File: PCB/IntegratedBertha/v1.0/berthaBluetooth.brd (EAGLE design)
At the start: 96.7 x 71.9 mm, 55 parts, among them CON1 SPI, Q1 BSP75, Q2 BSP75, Q4 BSP75, Q7 BSP75, X3 16MHz, X4 MINI-USB

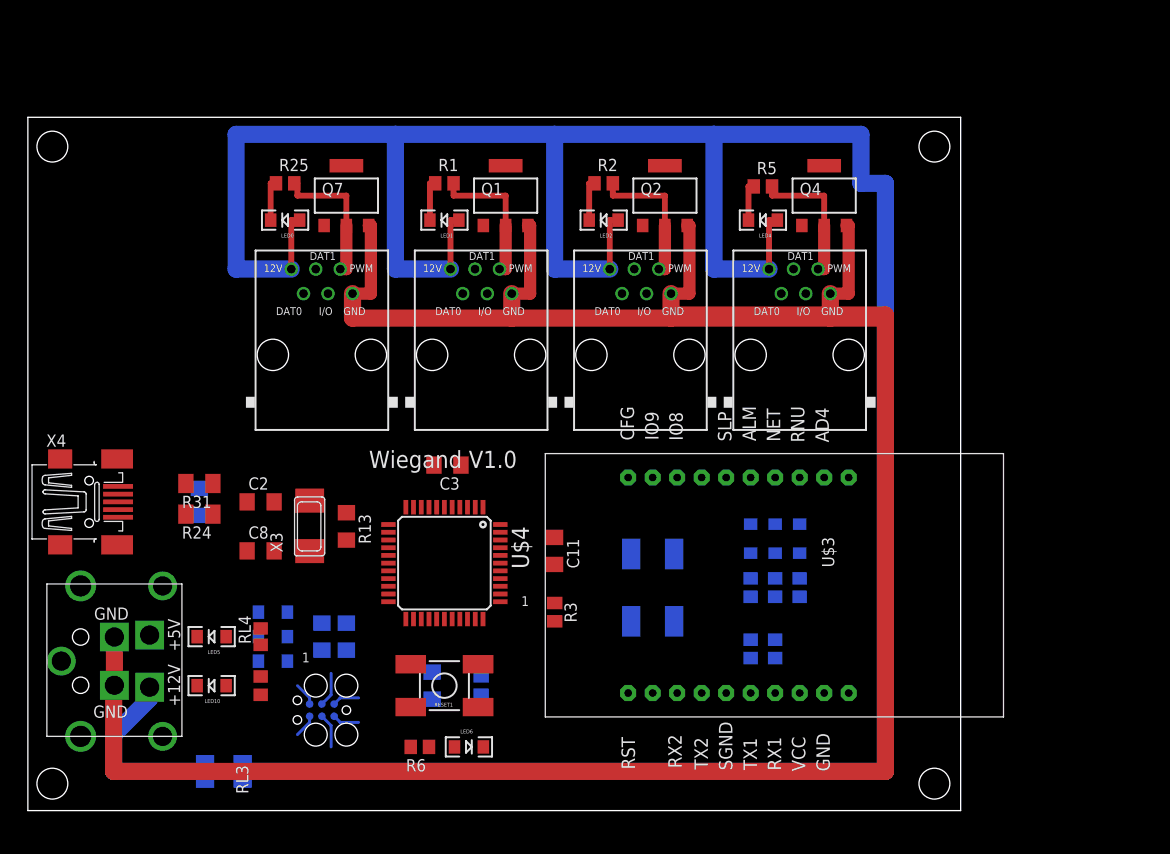
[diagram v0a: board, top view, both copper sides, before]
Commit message: Add relay card and integrated bioreactor
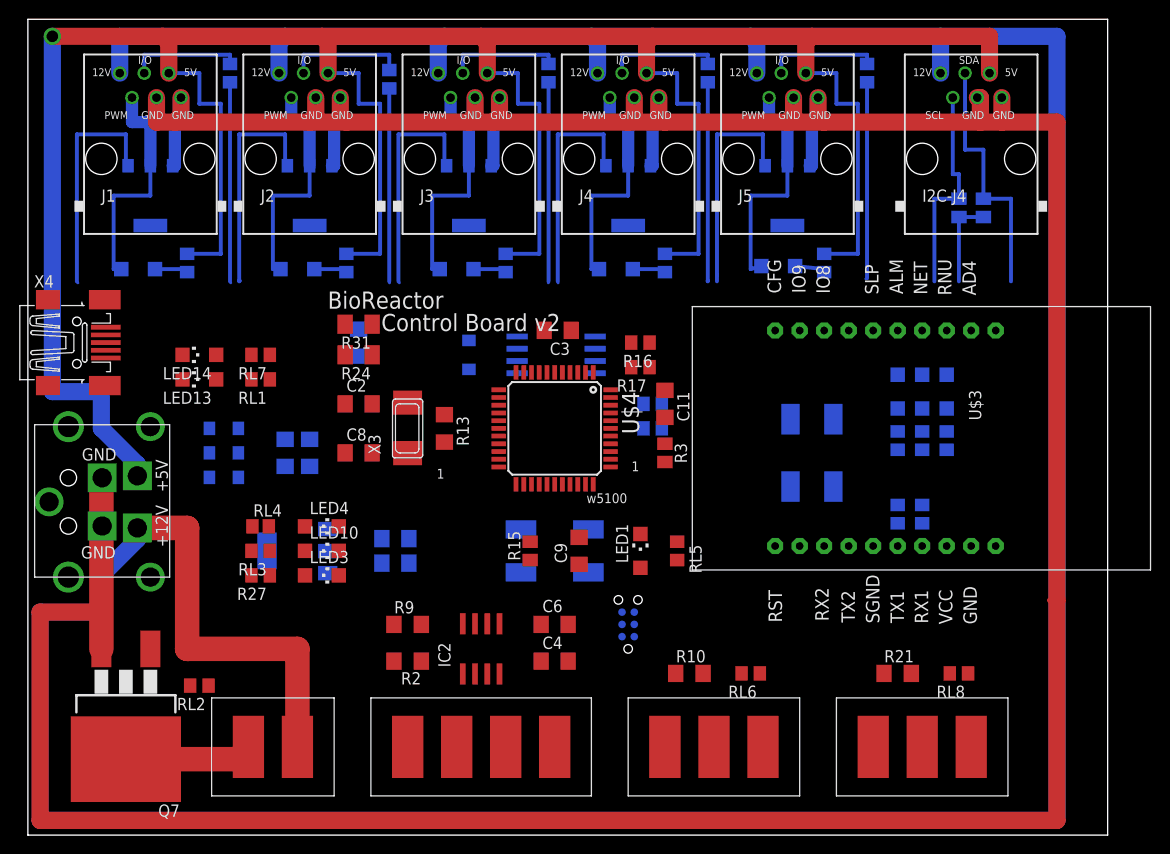
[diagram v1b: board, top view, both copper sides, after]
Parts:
- removed DOOR0, DOOR1, DOOR2, DOOR4: RJ12, lpatiny:RJ12-STRAIGHT-WIEGAND
- removed F1: 0.5A, lpatiny:C1812
- removed LED0: Blue, SparkFun:LED-1206
- added C1, C5: 10uF, rcl:C1206
- added C4: 100nF, rcl:C1206
- added C6: 330nF, rcl:C1206
- added D5: 1N581D1206, lpatiny:LED-1206
- added I2C-J4: RJ12STRAIGHT-I2C, lpatiny:RJ12-STRAIGHT-I2C
- added IC1: REG1117, burr-brown:SOT223
- added IC2: AD8223, analog-devices:SO8
- added J1, J2, J3, J4, J5: RJ12, lpatiny:RJ12-STRAIGHT
- added J7: 22--02, lpatiny:2-PIN-5.08S
- added LED13, LED3: RED, adafruit:CHIPLED_1206
- added LED14: GREEN, adafruit:CHIPLED_1206
- added LED7: BLue, adafruit:CHIPLED_1206
- added LED8: Blue, adafruit:CHIPLED_1206
- added Q5, Q6: BSP75, infineon:PG-SOT-223
- added R, R17, R32, R33, R34, R35, R4, R7: 1k, rcl:R0805
- added R10, R21: 4.7k, resistor:R1206
- added R16, R18: 10k, rcl:R0805
- added R27, RL1, RL2, RL5, RL6, RL7, RL8: 1K, rcl:R0805
- added R28, R29: 10K, resistor:M0805
- added R9: 100, resistor:R1206
- added U$1: SST25VF064C, BertaLib:SOIC_8-LEAD
- added X1: 22-23-20415.08S, lpatiny:4-PIN-5.08S
- added X2, X5: 22-23-20315.08S, lpatiny:3-PIN-5.08S
- CON1: device lpatiny:TC2030-MCP -> lpatiny:TC2030-MCP-NL
- LED1: value Blue -> GREEN; device SparkFun:LED-1206 -> adafruit:CHIPLED_1206
- LED10, LED11, LED12, LED2, LED9: device SparkFun:LED-1206 -> adafruit:CHIPLED_1206
- LED4: value Blue -> RED; device SparkFun:LED-1206 -> adafruit:CHIPLED_1206
- LED5, LED6: value RED -> Blue; device SparkFun:LED-1206 -> adafruit:CHIPLED_1206
- Q7: value BSP75 -> IRF3704S; device infineon:PG-SOT-223 -> transistor-power:D2PACK
- R2: value 10k -> 300; device rcl:R0805 -> resistor:R1206
- R25, R5: value 10k -> 1k
- R6: value 1K -> 1k
- U$4: value ATMEGA32U4 -> ATMEGA32U4-AU
- moved Q7 60.4 mm to (10.2, 7.62), turned to 180 degrees
- moved R6 56.2 mm to (66.0, 56.5), flipped to the bottom, turned to 90 degrees
- moved LED4 55.7 mm to (30.5, 29.2), turned to 270 degrees
- moved R2 53.5 mm to (39.4, 15.2), turned to 180 degrees
- moved LED6 49.5 mm to (44.5, 55.9), flipped to the bottom, turned to 270 degrees
- moved LED2 48.5 mm to (11.4, 55.9), flipped to the bottom, turned to 270 degrees
- moved LED1 39.9 mm to (63.5, 26.7), turned to 0 degrees
- moved LED5 39.1 mm to (27.9, 55.9), flipped to the bottom, turned to 270 degrees
- moved Q2 36.8 mm to (29.2, 63.5), flipped to the bottom, turned to 180 degrees
- moved Q1 36.8 mm to (12.7, 63.5), flipped to the bottom, turned to 180 degrees
- moved Q4 36.8 mm to (45.7, 63.5), flipped to the bottom, turned to 180 degrees
- moved R1 33.3 mm to (64.8, 39.4), flipped to the bottom, turned to 180 degrees
- moved CON1 29.9 mm to (62.2, 16.5), turned to 90 degrees
- moved R5 27.8 mm to (49.5, 56.5), flipped to the bottom, turned to 90 degrees
- moved R24 23.3 mm to (34.3, 47.0)
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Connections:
- removed net +5V1: R6.2
- removed net D2*: DOOR0.DAT0, U$4.19
- removed net D3*: DOOR0.DAT1, U$4.18
- removed net N$31: DOOR4.PWM, Q4.2, R5.2
- removed net N$39: F1.1, U$6.+12V
- new net 3.3V: C1.1, IC1.2, R1.2, R16.2, R27.2, U$1.RST/HOLD, U$1.VDD, U$1.WP
- new net DIFF+: IC2.3, X1.3
- new net DIFF-: IC2.2, X1.2
- new net FMOSI: D5.A, R1.1, U$1.SI
- new net N$10: R16.1, R17.1, U$1.CE
- new net N$13: IC2.1, R2.2
- new net N$14: LED14.A, RL7.2
- new net N$15: IC2.8, R2.1
- new net N$17: LED2.A, R25.1
- new net N$18: J1.I/O, R.2
- new net N$19: J5.PWM, LED8.C, Q6.2
- new net N$20: LED3.A, R27.1
- new net N$21: R10.2, RL6.2, X2.2
- new net N$22: LED6.A, R5.1
- new net N$28: J2.PWM, LED5.C, Q2.2
- new net N$29: J4.I/O, R34.2
- new net N$30: LED7.A, R6.1
- new net N$32: J5.I/O, R35.2
- new net N$33: LED8.A, R7.1
- new net N$34: J1.PWM, LED2.C, Q1.2
- new net N$36: J7.2, Q7.2
- new net N$4: LED5.A, R4.1
- new net N$40: IC2.6, R9.1
- new net N$8: LED13.A, RL1.2
- new net SCL: I2C-J4.SCL, R28.2, U$4.18
- new net SDA: I2C-J4.SDA, R29.2, U$4.19
- net +12V: now also I2C-J4.+12V, J1.+12V, J2.+12V, J3.+12V, J4.+12V, J5.+12V, J7.1, U$6.+12V; no longer DOOR0.+12V, DOOR1.+12V, DOOR2.+12V, DOOR4.+12V, F1.2, LED0.A, LED1.A, LED2.A, LED4.A
- net +5V: now also C4.1, I2C-J4.+5V, IC2.7, J1.+5V, J2.+5V, J3.+5V, J4.+5V, J5.+5V, R10.1, R21.1, R25.2, R28.1, R29.1, R4.2, R5.2, R6.2, R7.2, X1.1, X2.1, X5.1
- net +5V/1: now also C5.1, IC1.3
- net A0: now also R35.1; no longer DOOR4.I/O
- net A1: now also R33.1; no longer DOOR2.I/O
- net A2: now also R32.1; no longer DOOR1.I/O
- net A3: now also R.1; no longer DOOR0.I/O
- net A4: now also R34.1
- net A5: now also RL8.1
- net CS: now also R17.2
- net D10*: now also RL6.1; no longer DOOR2.DAT0
- net D11*: now also Q6.1; no longer DOOR2.DAT1
- net D12*: now also C6.1, R9.2; no longer Q4.1
- net D13*: now also RL5.1; no longer Q2.1
- net D5*: now also Q5.1; no longer Q1.1
- net D6*: now also Q1.1; no longer Q7.1
- net D7*: now also RL2.1
- net D8*: now also Q2.1; no longer DOOR1.DAT0
- net D9*: now also Q4.1; no longer DOOR1.DAT1
- net GND: now also C1.2, C4.2, C5.2, C6.2, I2C-J4.GND1, I2C-J4.GND2, IC1.1, IC2.4, IC2.5, J1.GND1, J1.GND2, J2.GND1, J2.GND2, J3.GND1, J3.GND2, J4.GND1, J4.GND2, J5.GND1, J5.GND2, LED1.C, LED13.C, LED14.C, LED3.C, LED4.C, Q5.3, Q6.3, U$1.VSS, X1.4, X2.3, X5.3; no longer DOOR0.GND, DOOR1.GND, DOOR2.GND, DOOR4.GND, LED5.C, LED6.C
- net MISO: now also U$1.SO; no longer DOOR4.DAT1
- net MOSI: now also D5.C
- net N$1: now also J3.PWM, LED6.C, Q4.2; no longer LED0.C, R25.1
- net N$12: now also LED4.A; no longer LED5.A
- net N$2: now also J2.I/O, R32.2; no longer LED6.A, R6.1
- net N$23: now also R18.2, U$1.SCK; no longer DOOR0.PWM, Q7.2, R25.2
- net N$3: now also LED1.A, RL5.2; no longer DOOR1.PWM, Q1.2, R1.2
- net N$5: now also J4.PWM, LED7.C, Q5.2; no longer LED1.C, R1.1
- net N$6: now also Q7.1, RL2.2; no longer LED2.C, R2.1
- net N$7: now also J3.I/O, R33.2; no longer DOOR2.PWM, Q2.2, R2.2
- net N$9: now also R21.2, RL8.2, X5.2; no longer LED4.C, R5.1
- net RD+: now also RL7.1
- net RD-: now also RL1.1
- net SCK: now also R18.1; no longer DOOR4.DAT0
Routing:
- net +5V: track 0.00 -> 320.9 mm, vias 0 -> 1
- net GND: track 269.0 -> 404.4 mm
- net +12V: track 302.5 -> 385.3 mm
- net SDA: track 0.00 -> 26.4 mm
- net N$19: track 0.00 -> 24.6 mm
- net N$28: track 0.00 -> 24.3 mm
- net N$34: track 0.00 -> 24.3 mm
- net D6*: track 0.00 -> 24.0 mm
- net D9*: track 0.00 -> 23.7 mm
- net D5*: track 0.00 -> 23.6 mm
- net D8*: track 0.00 -> 23.6 mm
- net D11*: track 0.00 -> 23.5 mm
- net SCL: track 0.00 -> 22.2 mm
- net A3: track 0.00 -> 20.8 mm
- net A1: track 0.00 -> 20.8 mm
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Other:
- board size 96.7 x 71.9 mm -> 111.9 x 84.6 mm
- board text added: "-"
- board text added: "5V"
- board text added: "BioReactor"
- board text added: "Control Board v2"
- board text added: "DAT"
- board text added: "GND"
- board text added: "PID"
- board text added: "Tliquid"
- board text added: "Tplate"
- board text added: "Weight"
- board text added: "XX"
- board text added: "w5100"
- board text removed: "Wiegand V1.0"
- board text removed: "Wiegand v1.1"
